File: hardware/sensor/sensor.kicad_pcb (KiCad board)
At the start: 2 copper layers, 73 x 32 mm, 39 parts, among them IC1 STM8L001J3M3, IC2 Si4012-C1001GTR, IC3 TPS3839L30DBZR, J1 M20-9770342

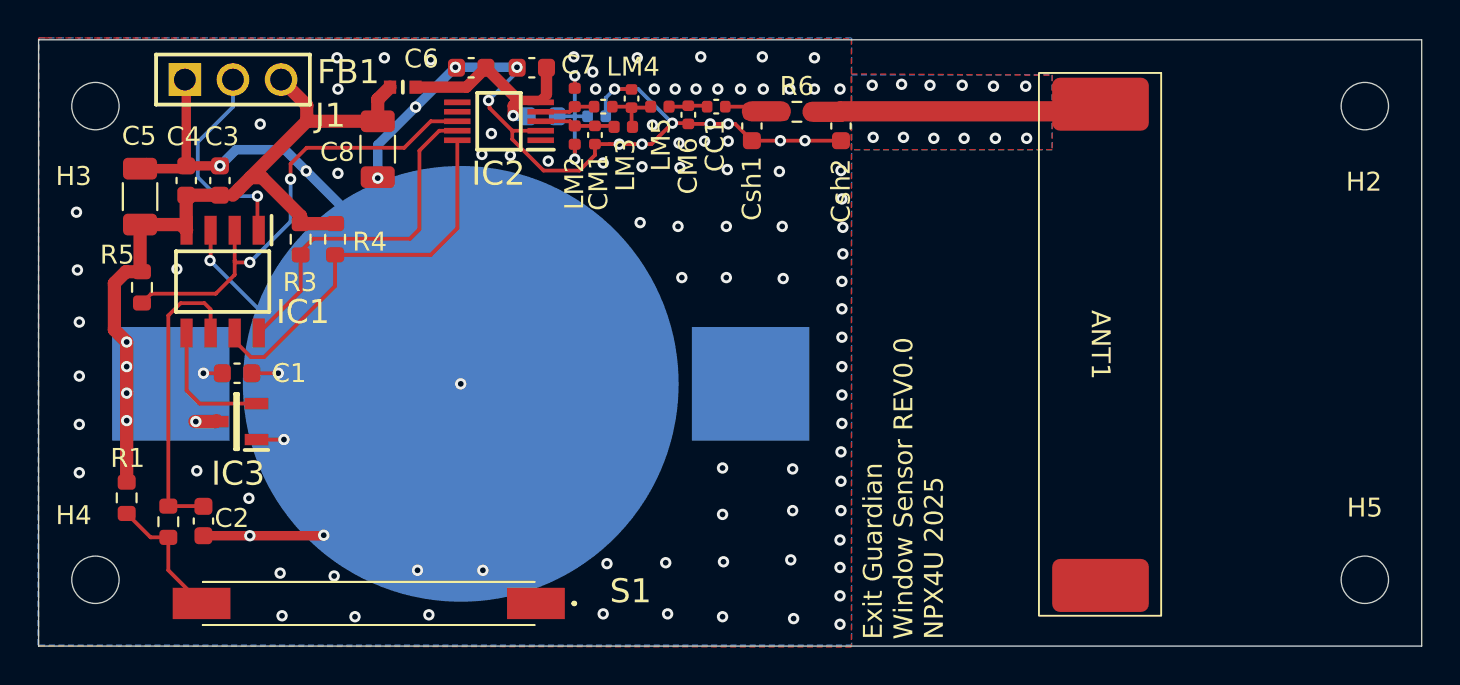
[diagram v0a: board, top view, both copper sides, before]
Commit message: EG-34 PCB antenna PI removed and added vias to connect ground planes on battery holder place.
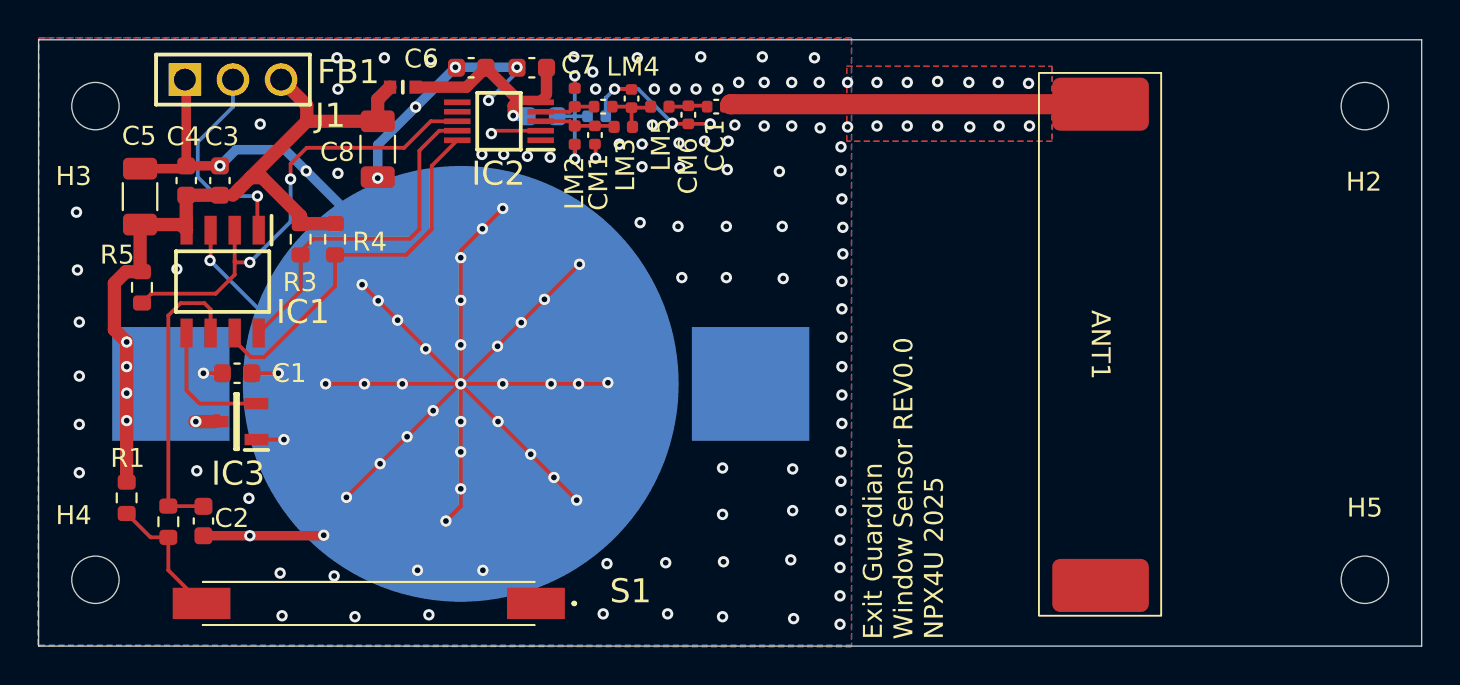
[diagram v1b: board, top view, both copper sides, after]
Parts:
- removed Csh1, Csh2: NC, Capacitor_SMD:C_0603_1608Metric
- removed R6: 0, Resistor_SMD:R_0603_1608Metric
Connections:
- CC1 pad 1: Net-(CC1-Pad1) -> Net-(ANT1-Pad1)
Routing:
- net GND: track 131.6 -> 180.0 mm, vias 120 -> 156
- net Net-(ANT1-Pad1): track 15.4 -> 20.4 mm
- net Net-(CC1-Pad1): track 3.15 -> 0.00 mm
- net SDA: track 21.4 -> 20.6 mm

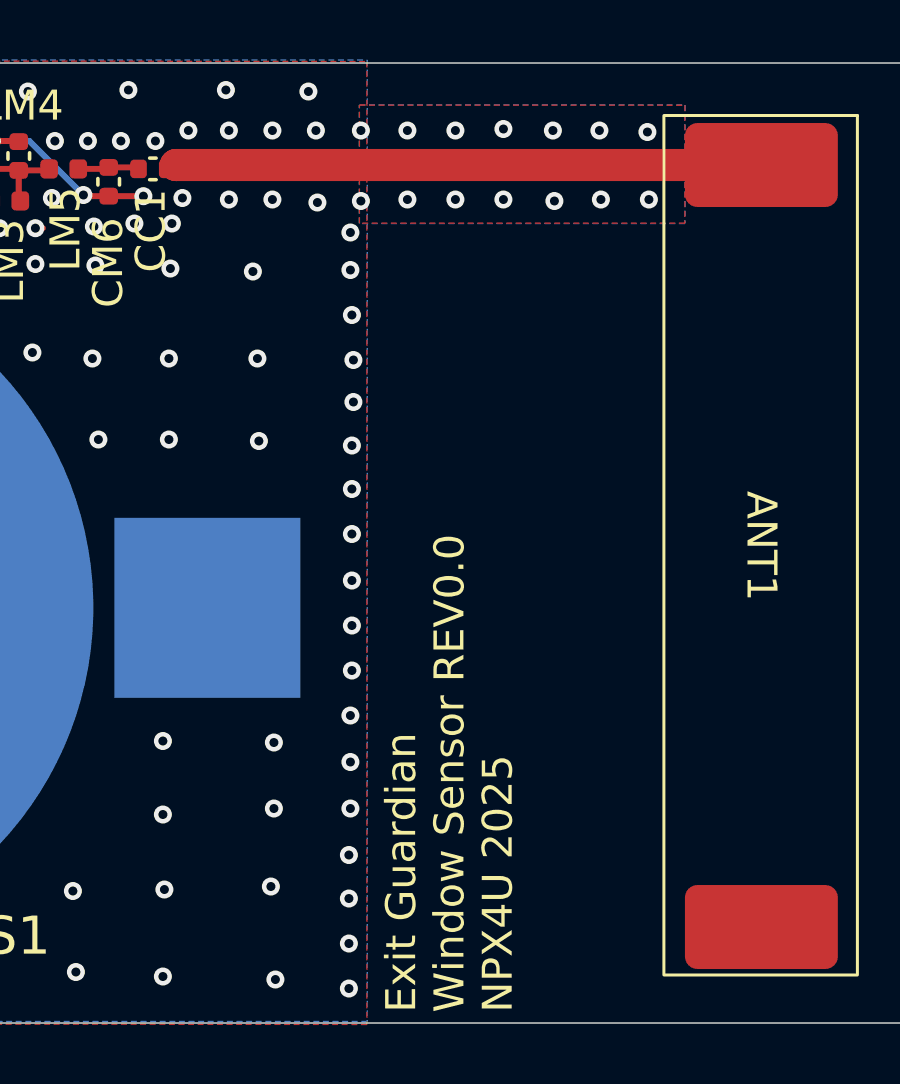
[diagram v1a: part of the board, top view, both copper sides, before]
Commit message: EG-34 Fixed the revision and PCB name on silkscreen.
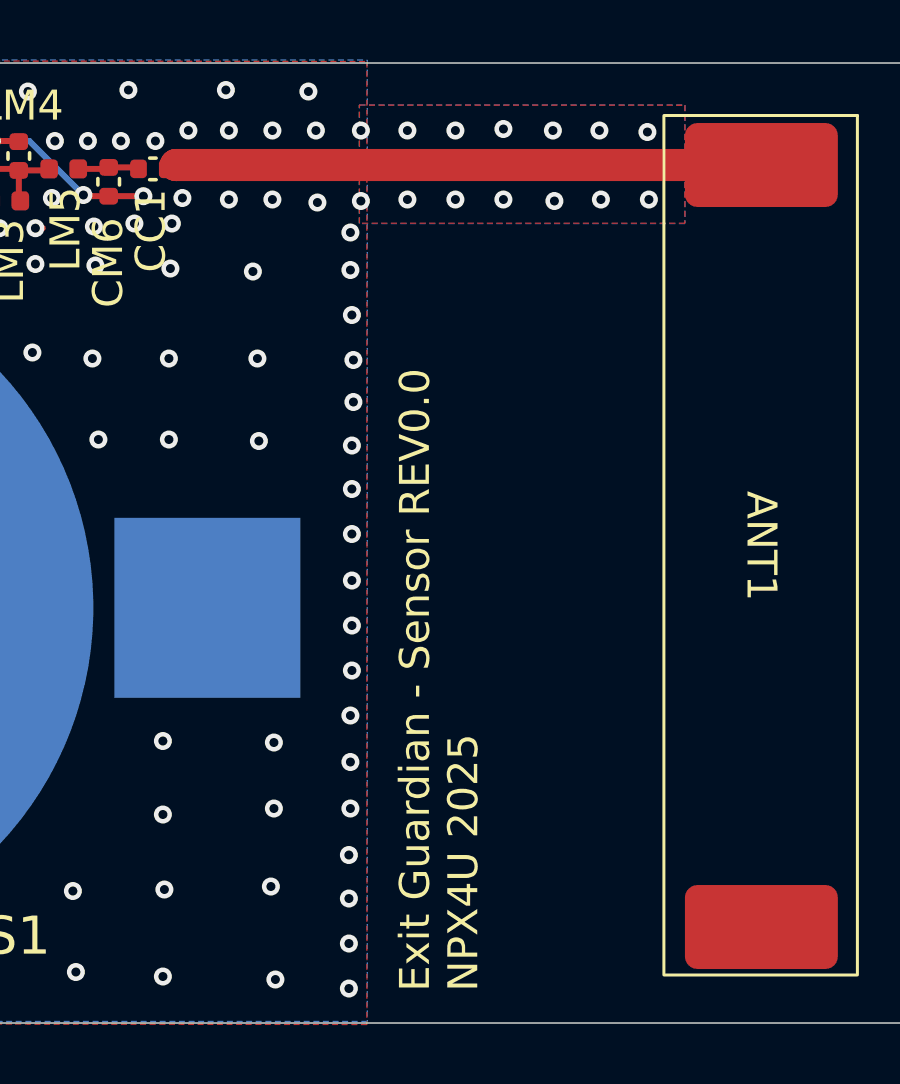
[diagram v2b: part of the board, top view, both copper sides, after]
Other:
- board text added: "Exit Guardian - Sensor REV0.0 NPX4U 2025"
- board text removed: "Exit Guardian Window Sensor REV0.0 NPX4U 2025"
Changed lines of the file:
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@@
 		(layer "Edge.Cuts")
 	)
-	(gr_text "Exit Guardian\nWindow Sensor REV0.0\nNPX4U 2025"
-		(at 224.65 161.05 90)
+	(gr_text "Exit Guardian - Sensor REV0.0\nNPX4U 2025"
+		(at 223.5 160.35 90)
 		(layer "F.SilkS")
 		(effects

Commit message: EG-37 Gerbers, drills, position and BOM generated.
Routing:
- net GND: track 180.0 -> 193.8 mm, vias 156 -> 157
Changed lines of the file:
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@@
 			(outputformat 1)
 			(mirror no)
-			(drillshape 1)
+			(drillshape 0)
 			(scaleselection 1)
-			(outputdirectory "")
+			(outputdirectory "output/")
 		)
 	)
@@
 		(sheetname "/")
 		(sheetfile "sensor.kicad_sch")
-		(attr through_hole)
+		(attr through_hole dnp)
 		(fp_line
 			(start -1.52 -1.32)
@@
 	)
 	(via
+		(at 193.725 139.125)
+		(size 0.6)
+		(drill 0.3)
+		(layers "F.Cu" "B.Cu")
+		(net 1)
+	)
+	(via
 		(at 221.05 131.65)
 		(size 0.6)
@@
 	)
 	(segment
-		(start 199.082 147.45)
-		(end 199.082 147.56)
-		(width 0.5)
-		(layer "B.Cu")
-		(net 1)
-	)
-	(segment
 		(start 187.2254 135.2)
 		(end 189.8 135.2)
@@
 	(segment
 		(start 190.925 136.325)
-		(end 199.082 144.482)
+		(end 193.725 139.125)
 		(width 0.5)
 		(layer "B.Cu")
@@
 	)
 	(segment
+		(start 193.725 142.203)
+		(end 199.082 147.56)
+		(width 0.5)
+		(layer "B.Cu")
+		(net 1)
+	)
+	(segment
 		(start 189.45 147)
 		(end 198.522 147)
@@
 	)
 	(segment
-		(start 199.082 144.482)
-		(end 199.082 147.45)
+		(start 199.082 142.932)
+		(end 192.6 136.45)
 		(width 0.5)
 		(layer "B.Cu")
@@
 		(layer "B.Cu")
 		(net 1)
+	)
+	(segment
+		(start 193.725 139.125)
+		(end 193.725 142.203)
+		(width 0.5)
+		(layer "B.Cu")
+		(net 1)
+	)
+	(segment
+		(start 199.082 147.56)
+		(end 199.082 142.932)
+		(width 0.5)
+		(layer "B.Cu")
+		(net 1)
